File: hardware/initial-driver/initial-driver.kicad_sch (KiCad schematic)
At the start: 9 parts, among them J1 PWR_IN, J2 MOTOR, J3 BREAK, J4 USB_C, U1 ESP32-S3-WROOM-1

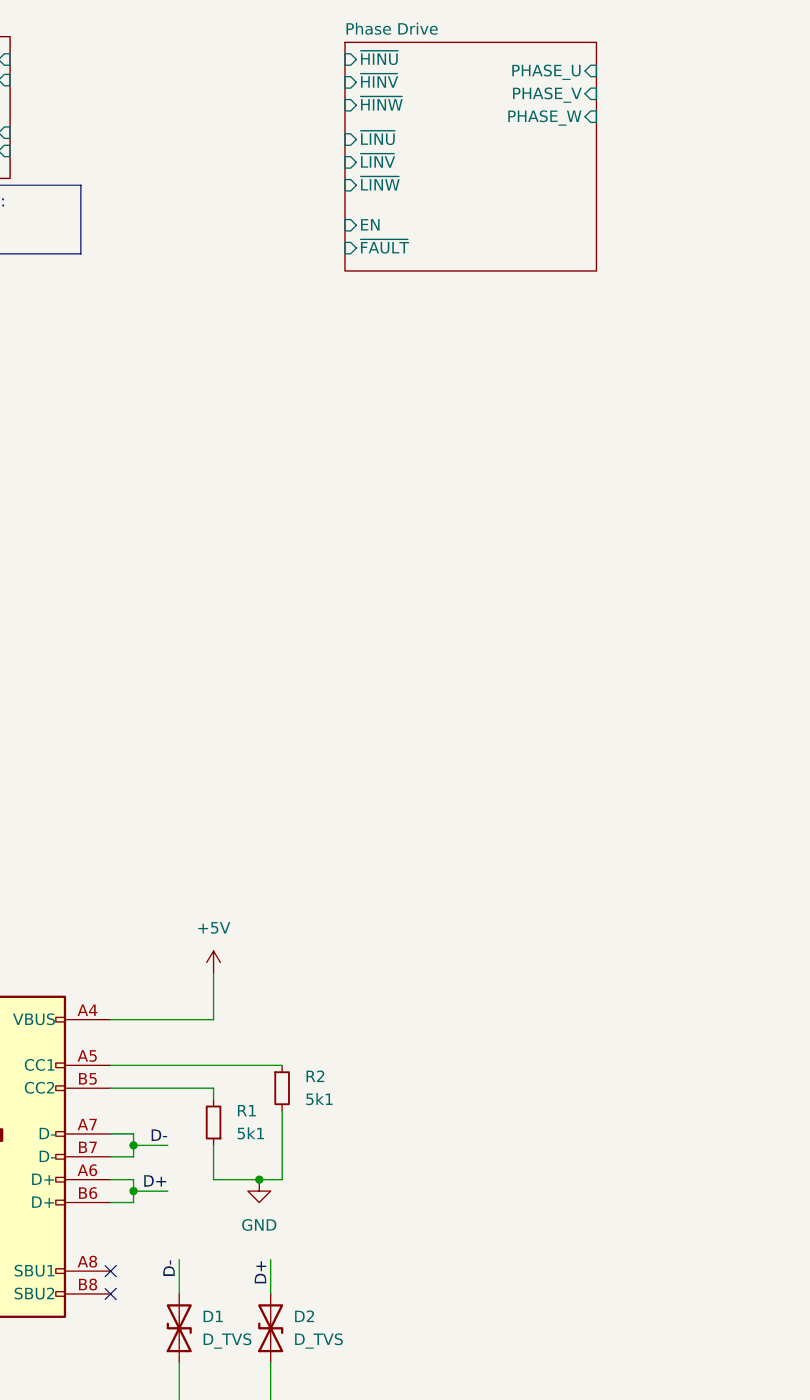
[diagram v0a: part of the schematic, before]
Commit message: Refactor current sensing
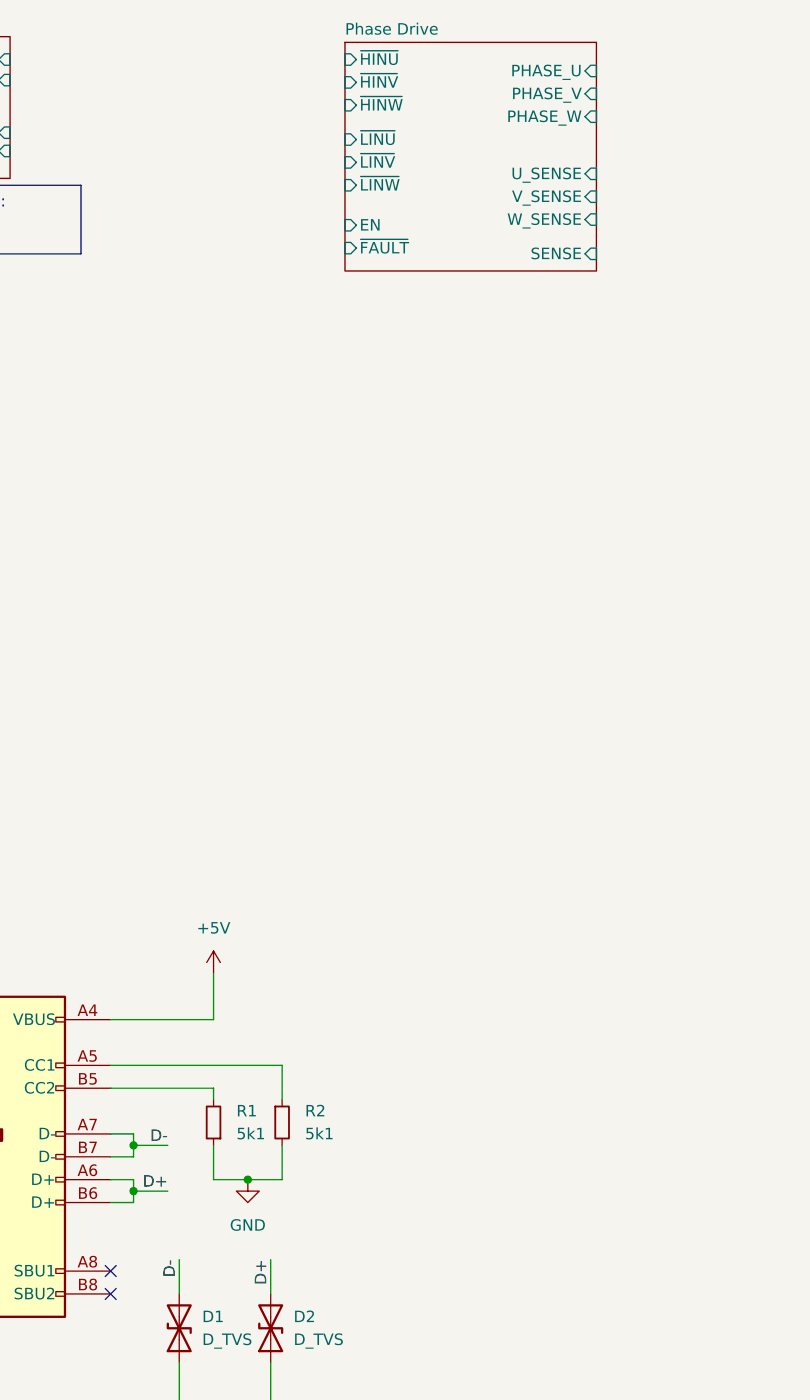
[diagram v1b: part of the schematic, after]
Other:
- sheet Phase Drive ports: added SENSE, U_SENSE, V_SENSE, W_SENSE; removed none
- moved on the sheet: R2
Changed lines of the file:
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@@
 (kicad_sch (version 20230121) (generator eeschema)
   (paper "A4")
+  (junction (at 66.04 149.86) (diameter 0) (color 0 0 0 0)
+  )
   (junction (at 30.48 176.53) (diameter 0) (color 0 0 0 0)
-  )
-  (junction (at 67.31 149.86) (diameter 0) (color 0 0 0 0)
   )
   (junction (at 63.5 176.53) (diameter 0) (color 0 0 0 0)
@@
     (stroke (width 0) (type default))
   )
-  (wire (pts (xy 69.85 149.86) (xy 69.85 142.24))
+  (wire (pts (xy 69.85 149.86) (xy 69.85 146.05))
     (stroke (width 0) (type default))
   )
@@
     (stroke (width 0) (type default))
   )
+  (wire (pts (xy 50.8 137.16) (xy 69.85 137.16))
+    (stroke (width 0) (type default))
+  )
   (wire (pts (xy 63.5 176.53) (xy 68.58 176.53))
     (stroke (width 0) (type default))
   )
+  (wire (pts (xy 66.04 149.86) (xy 69.85 149.86))
+    (stroke (width 0) (type default))
+  )
   (wire (pts (xy 246.38 41.91) (xy 254 41.91))
     (stroke (width 0) (type default))
@@
     (stroke (width 0) (type default))
   )
-  (wire (pts (xy 67.31 149.86) (xy 62.23 149.86))
-    (stroke (width 0) (type default))
-  )
   (wire (pts (xy 246.38 39.37) (xy 254 39.37))
     (stroke (width 0) (type default))
   )
+  (wire (pts (xy 69.85 137.16) (xy 69.85 140.97))
+    (stroke (width 0) (type default))
+  )
   (wire (pts (xy 246.38 24.13) (xy 254 24.13))
     (stroke (width 0) (type default))
@@
     (stroke (width 0) (type default))
   )
-  (wire (pts (xy 50.8 137.16) (xy 69.85 137.16))
-    (stroke (width 0) (type default))
-  )
-  (wire (pts (xy 67.31 149.86) (xy 69.85 149.86))
-    (stroke (width 0) (type default))
-  )
   (wire (pts (xy 50.8 144.78) (xy 53.34 144.78))
     (stroke (width 0) (type default))
@@
   )
   (wire (pts (xy 53.34 151.13) (xy 53.34 152.4))
+    (stroke (width 0) (type default))
+  )
+  (wire (pts (xy 66.04 149.86) (xy 62.23 149.86))
     (stroke (width 0) (type default))
   )
@@
     )
   )
-  (symbol (lib_id "Device:R_Small") (at 69.85 139.7 0) (unit 1)
-    (in_bom yes) (on_board yes) (dnp no) (fields_autoplaced)
-    (property "Reference" "R2" (at 72.39 138.43 0)
-      (effects (font (size 1.27 1.27)) (justify left))
-    )
-    (property "Value" "5k1" (at 72.39 140.97 0)
-      (effects (font (size 1.27 1.27)) (justify left))
-    )
-    (property "Footprint" "" (at 69.85 139.7 0)
-      (effects (font (size 1.27 1.27)) hide)
-    )
-    (property "Datasheet" "~" (at 69.85 139.7 0)
+  (symbol (lib_id "Device:R_Small") (at 69.85 143.51 0) (unit 1)
+    (in_bom yes) (on_board yes) (dnp no) (fields_autoplaced)
+    (property "Reference" "R2" (at 72.39 142.24 0)
+      (effects (font (size 1.27 1.27)) (justify left))
+    )
+    (property "Value" "5k1" (at 72.39 144.78 0)
+      (effects (font (size 1.27 1.27)) (justify left))
+    )
+    (property "Footprint" "" (at 69.85 143.51 0)
+      (effects (font (size 1.27 1.27)) hide)
+    )
+    (property "Datasheet" "~" (at 69.85 143.51 0)
       (effects (font (size 1.27 1.27)) hide)
     )
@@
     )
   )
-  (symbol (lib_id "power:GND") (at 67.31 149.86 0) (unit 1)
-    (in_bom yes) (on_board yes) (dnp no) (fields_autoplaced)
-    (property "Reference" "#PWR06" (at 67.31 156.21 0)
-      (effects (font (size 1.27 1.27)) hide)
-    )
-    (property "Value" "GND" (at 67.31 154.94 0)
-      (effects (font (size 1.27 1.27)))
-    )
-    (property "Footprint" "" (at 67.31 149.86 0)
-      (effects (font (size 1.27 1.27)) hide)
-    )
-    (property "Datasheet" "" (at 67.31 149.86 0)
+  (symbol (lib_id "power:GND") (at 66.04 149.86 0) (unit 1)
+    (in_bom yes) (on_board yes) (dnp no) (fields_autoplaced)
+    (property "Reference" "#PWR06" (at 66.04 156.21 0)
+      (effects (font (size 1.27 1.27)) hide)
+    )
+    (property "Value" "GND" (at 66.04 154.94 0)
+      (effects (font (size 1.27 1.27)))
+    )
+    (property "Footprint" "" (at 66.04 149.86 0)
+      (effects (font (size 1.27 1.27)) hide)
+    )
+    (property "Datasheet" "" (at 66.04 149.86 0)
       (effects (font (size 1.27 1.27)) hide)
     )
@@
       (effects (font (size 1.27 1.27)) (justify left))
     )
-    (instances
+    (pin "SENSE" input (at 104.775 46.99 0)
+      (effects (font (size 1.27 1.27)) (justify right))
+    )
+    (pin "V_SENSE" input (at 104.775 40.64 0)
+      (effects (font (size 1.27 1.27)) (justify right))
+    )
+    (pin "W_SENSE" input (at 104.775 43.18 0)
+      (effects (font (size 1.27 1.27)) (justify right))
+    )
+    (pin "U_SENSE" input (at 104.775 38.1 0)
+      (effects (font (size 1.27 1.27)) (justify right))
+    )
+    (instances

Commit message: updated more stuff
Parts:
- added U9: SN65HVD230, Package_SO:SOIC-8_3.9x4.9mm_P1.27mm, symbol Interface_CAN_LIN:SN65HVD230
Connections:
- net +3V3: now also U9.3 (VCC)
- net GND: now also U9.2 (GND), U9.8 (Rs)
- net CAN_TDX: now reaches U1.11 (GPIO18/U1RXD/ADC2_CH7/CLK_OUT3)
- net CAN_TDX: now also U9.1 (D)
- net CAN_RXD: now reaches U1.23 (GPIO21)
- net CAN_RXD: now also U9.4 (R)
- new net CANH: U9.7 (CANH)
- new net CANL: U9.6 (CANL)
- no-connect marks 2 -> 3

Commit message: add more stuff
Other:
- moved on the sheet: U1
